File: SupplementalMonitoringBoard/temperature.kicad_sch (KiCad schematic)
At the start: 11 parts, among them U3 INA180B1

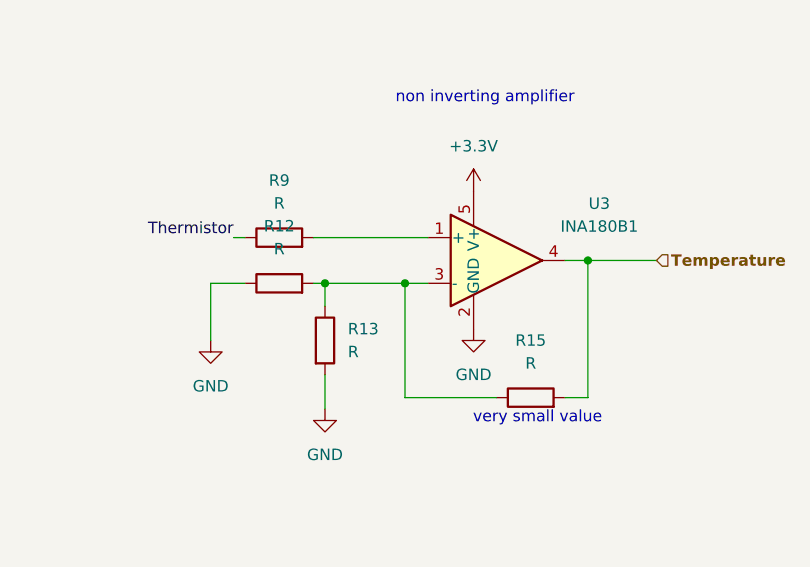
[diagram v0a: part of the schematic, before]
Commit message: Supplemental Monitoring Board Changes
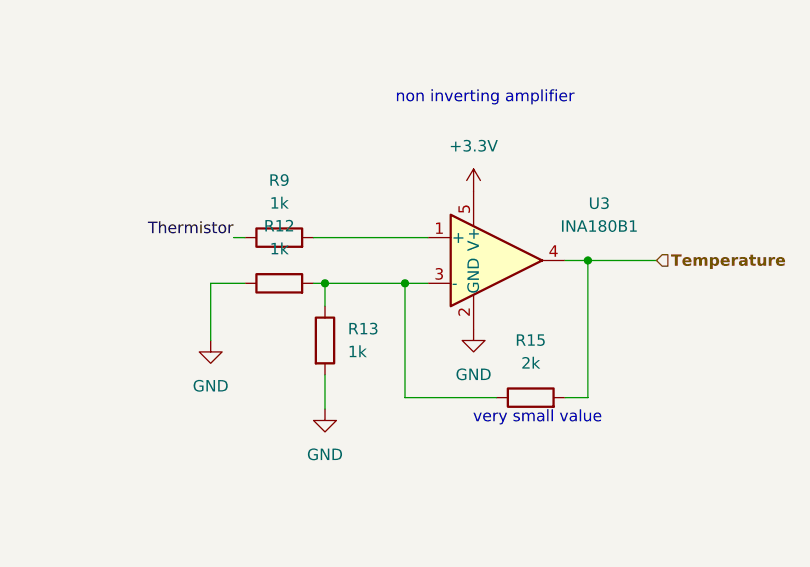
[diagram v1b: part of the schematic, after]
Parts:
- R12, R13, R9: value R -> 1k
- R15: value R -> 2k
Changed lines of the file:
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@@
 			)
 		)
-		(property "Value" "R"
+		(property "Value" "1k"
 			(at 127 87.63 90)
 			(effects
@@
 			)
 		)
-		(property "Value" "R"
+		(property "Value" "1k"
 			(at 134.62 104.1399 0)
 			(effects
@@
 			)
 		)
-		(property "Value" "R"
+		(property "Value" "2k"
 			(at 154.94 105.41 90)
 			(effects
@@
 			)
 		)
-		(property "Value" "R"
+		(property "Value" "1k"
 			(at 127 92.71 90)
 			(effects
